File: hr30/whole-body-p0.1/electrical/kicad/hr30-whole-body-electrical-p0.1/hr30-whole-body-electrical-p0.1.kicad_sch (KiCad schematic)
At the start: 0 parts

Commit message: Expand HR-30 whole-body electrical architecture
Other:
- sheet 12 Head TTL, sensing, display and audio renamed 12 Head TTL, cameras, face display, audio and cooling
- added sheet 13 Auxiliary conversion and pelvis inertial sensing (13_pelvis_aux_imu.kicad_sch)
- added sheet 14 Left foot four-point load sensing (14_left_foot_load_sensing.kicad_sch)
- added sheet 15 Right foot four-point load sensing (15_right_foot_load_sensing.kicad_sch)

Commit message: Add pin-level HR-30 actuator interface carriers
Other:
- removed sheet 04 Five isolated RS-485 and three protected TTL interface channels
- removed sheet 05 Left-leg RS-485 and protected branch
- removed sheet 06 Right-leg RS-485 and protected branch
- removed sheet 07 Left proximal-arm RS-485 and protected branch
- removed sheet 08 Right proximal-arm RS-485 and protected branch
- removed sheet 09 Waist RS-485 and protected branch
- removed sheet 10 Left wrist/gripper TTL and protected branch
- removed sheet 11 Right wrist/gripper TTL and protected branch
- removed sheet 12 Head TTL, cameras, face display, audio and cooling
- removed sheet 13 Auxiliary conversion and pelvis inertial sensing
- removed sheet 14 Left foot four-point load sensing
- removed sheet 15 Right foot four-point load sensing
- added sheet 04 STM32H743 motion-controller power and carrier connectors (04_motion_controller_carrier_connectors.kicad_sch)
- added sheet 05 Carrier A - four isolated RS-485 channels (05_carrier_a_four_isolated_rs485.kicad_sch)
- added sheet 06 Carrier B - waist RS-485 and three translated TTL channels (06_carrier_b_waist_and_ttl.kicad_sch)
- added sheet 07 Left-leg RS-485 and protected branch (07_left_leg_rs485.kicad_sch)
- added sheet 08 Right-leg RS-485 and protected branch (08_right_leg_rs485.kicad_sch)
- added sheet 09 Left proximal-arm RS-485 and protected branch (09_left_arm_rs485.kicad_sch)
- added sheet 10 Right proximal-arm RS-485 and protected branch (10_right_arm_rs485.kicad_sch)
- added sheet 11 Waist RS-485 and protected branch (11_waist_rs485.kicad_sch)
- added sheet 12 Left wrist/gripper TTL and protected branch (12_left_distal_ttl.kicad_sch)
- added sheet 13 Right wrist/gripper TTL and protected branch (13_right_distal_ttl.kicad_sch)
- added sheet 14 Head TTL, cameras, face display, audio and cooling (14_head_ttl_sensors_hmi.kicad_sch)
- added sheet 15 Auxiliary conversion and pelvis inertial sensing (15_pelvis_aux_imu.kicad_sch)
- added sheet 16 Left foot four-point load sensing (16_left_foot_load_sensing.kicad_sch)
- added sheet 17 Right foot four-point load sensing (17_right_foot_load_sensing.kicad_sch)

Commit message: Correct HR-30 whole-body electrical architecture
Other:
- sheet 01 Energy, service disconnect, precharge and conversion renamed 01 Tether-first energy, regulated rails and onboard-later boundary
- sheet 07 Left-leg RS-485 and protected branch renamed 07 Left-leg RS-485 data bus and individual feeds
- sheet 08 Right-leg RS-485 and protected branch renamed 08 Right-leg RS-485 data bus and individual feeds
- sheet 09 Left proximal-arm RS-485 and protected branch renamed 09 Left proximal-arm RS-485 data bus and individual feeds
- sheet 10 Right proximal-arm RS-485 and protected branch renamed 10 Right proximal-arm RS-485 data bus and individual feeds
- sheet 11 Waist RS-485 and protected branch renamed 11 Waist RS-485 data bus and individual feed
- sheet 12 Left wrist/gripper TTL and protected branch renamed 12 Left wrist/gripper TTL data bus and individual feeds
- sheet 13 Right wrist/gripper TTL and protected branch renamed 13 Right wrist/gripper TTL data bus and individual feeds
- added sheet 18 Onboard-later isolated energy evaluation (18_onboard_later_energy_evaluation.kicad_sch)
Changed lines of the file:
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@@
           (exclude_from_sim no) (in_bom yes) (on_board yes) (dnp no)
           (stroke (width 0.5) (type solid)) (fill (color 0 0 0 0.0000))
-          (property "Sheetname" "01 Energy, service disconnect, precharge and conversion" (at 14.54 48.16 0) (effects (font (size 1.50 1.50)) (justify left bottom)))
+          (property "Sheetname" "01 Tether-first energy, regulated rails and onboard-later boundary" (at 14.54 48.16 0) (effects (font (size 1.50 1.50)) (justify left bottom)))
           (property "Sheetfile" "01_energy_precharge_conversion.kicad_sch" (at 14.54 63.40 0) (effects (font (size 1.30 1.30)) (justify left top)))
           (instances (project "hr30-whole-body-electrical-p0.1" (path "/6dbc6f1c-d05b-56f0-8b51-042e5f8599ba" (page "2"))))) (sheet (at 112.00 38.00) (size 92.0 40.64)
@@
           (exclude_from_sim no) (in_bom yes) (on_board yes) (dnp no)
           (stroke (width 0.5) (type solid)) (fill (color 0 0 0 0.0000))
-          (property "Sheetname" "07 Left-leg RS-485 and protected branch" (at 214.54 98.16 0) (effects (font (size 1.50 1.50)) (justify left bottom)))
+          (property "Sheetname" "07 Left-leg RS-485 data bus and individual feeds" (at 214.54 98.16 0) (effects (font (size 1.50 1.50)) (justify left bottom)))
           (property "Sheetfile" "07_left_leg_rs485.kicad_sch" (at 214.54 113.40 0) (effects (font (size 1.30 1.30)) (justify left top)))
           (instances (project "hr30-whole-body-electrical-p0.1" (path "/6dbc6f1c-d05b-56f0-8b51-042e5f8599ba" (page "8"))))) (sheet (at 312.00 88.00) (size 92.0 40.64)
           (exclude_from_sim no) (in_bom yes) (on_board yes) (dnp no)
           (stroke (width 0.5) (type solid)) (fill (color 0 0 0 0.0000))
-          (property "Sheetname" "08 Right-leg RS-485 and protected branch" (at 314.54 98.16 0) (effects (font (size 1.50 1.50)) (justify left bottom)))
+          (property "Sheetname" "08 Right-leg RS-485 data bus and individual feeds" (at 314.54 98.16 0) (effects (font (size 1.50 1.50)) (justify left bottom)))
           (property "Sheetfile" "08_right_leg_rs485.kicad_sch" (at 314.54 113.40 0) (effects (font (size 1.30 1.30)) (justify left top)))
           (instances (project "hr30-whole-body-electrical-p0.1" (path "/6dbc6f1c-d05b-56f0-8b51-042e5f8599ba" (page "9"))))) (sheet (at 12.00 138.00) (size 92.0 40.64)
           (exclude_from_sim no) (in_bom yes) (on_board yes) (dnp no)
           (stroke (width 0.5) (type solid)) (fill (color 0 0 0 0.0000))
-          (property "Sheetname" "09 Left proximal-arm RS-485 and protected branch" (at 14.54 148.16 0) (effects (font (size 1.50 1.50)) (justify left bottom)))
+          (property "Sheetname" "09 Left proximal-arm RS-485 data bus and individual feeds" (at 14.54 148.16 0) (effects (font (size 1.50 1.50)) (justify left bottom)))
           (property "Sheetfile" "09_left_arm_rs485.kicad_sch" (at 14.54 163.40 0) (effects (font (size 1.30 1.30)) (justify left top)))
           (instances (project "hr30-whole-body-electrical-p0.1" (path "/6dbc6f1c-d05b-56f0-8b51-042e5f8599ba" (page "10"))))) (sheet (at 112.00 138.00) (size 92.0 40.64)
           (exclude_from_sim no) (in_bom yes) (on_board yes) (dnp no)
           (stroke (width 0.5) (type solid)) (fill (color 0 0 0 0.0000))
-          (property "Sheetname" "10 Right proximal-arm RS-485 and protected branch" (at 114.54 148.16 0) (effects (font (size 1.50 1.50)) (justify left bottom)))
+          (property "Sheetname" "10 Right proximal-arm RS-485 data bus and individual feeds" (at 114.54 148.16 0) (effects (font (size 1.50 1.50)) (justify left bottom)))
           (property "Sheetfile" "10_right_arm_rs485.kicad_sch" (at 114.54 163.40 0) (effects (font (size 1.30 1.30)) (justify left top)))
           (instances (project "hr30-whole-body-electrical-p0.1" (path "/6dbc6f1c-d05b-56f0-8b51-042e5f8599ba" (page "11"))))) (sheet (at 212.00 138.00) (size 92.0 40.64)
           (exclude_from_sim no) (in_bom yes) (on_board yes) (dnp no)
           (stroke (width 0.5) (type solid)) (fill (color 0 0 0 0.0000))
-          (property "Sheetname" "11 Waist RS-485 and protected branch" (at 214.54 148.16 0) (effects (font (size 1.50 1.50)) (justify left bottom)))
+          (property "Sheetname" "11 Waist RS-485 data bus and individual feed" (at 214.54 148.16 0) (effects (font (size 1.50 1.50)) (justify left bottom)))
           (property "Sheetfile" "11_waist_rs485.kicad_sch" (at 214.54 163.40 0) (effects (font (size 1.30 1.30)) (justify left top)))
           (instances (project "hr30-whole-body-electrical-p0.1" (path "/6dbc6f1c-d05b-56f0-8b51-042e5f8599ba" (page "12"))))) (sheet (at 312.00 138.00) (size 92.0 40.64)
           (exclude_from_sim no) (in_bom yes) (on_board yes) (dnp no)
           (stroke (width 0.5) (type solid)) (fill (color 0 0 0 0.0000))
-          (property "Sheetname" "12 Left wrist/gripper TTL and protected branch" (at 314.54 148.16 0) (effects (font (size 1.50 1.50)) (justify left bottom)))
+          (property "Sheetname" "12 Left wrist/gripper TTL data bus and individual feeds" (at 314.54 148.16 0) (effects (font (size 1.50 1.50)) (justify left bottom)))
           (property "Sheetfile" "12_left_distal_ttl.kicad_sch" (at 314.54 163.40 0) (effects (font (size 1.30 1.30)) (justify left top)))
           (instances (project "hr30-whole-body-electrical-p0.1" (path "/6dbc6f1c-d05b-56f0-8b51-042e5f8599ba" (page "13"))))) (sheet (at 12.00 188.00) (size 92.0 40.64)
           (exclude_from_sim no) (in_bom yes) (on_board yes) (dnp no)
           (stroke (width 0.5) (type solid)) (fill (color 0 0 0 0.0000))
-          (property "Sheetname" "13 Right wrist/gripper TTL and protected branch" (at 14.54 198.16 0) (effects (font (size 1.50 1.50)) (justify left bottom)))
+          (property "Sheetname" "13 Right wrist/gripper TTL data bus and individual feeds" (at 14.54 198.16 0) (effects (font (size 1.50 1.50)) (justify left bottom)))
           (property "Sheetfile" "13_right_distal_ttl.kicad_sch" (at 14.54 213.40 0) (effects (font (size 1.30 1.30)) (justify left top)))
           (instances (project "hr30-whole-body-electrical-p0.1" (path "/6dbc6f1c-d05b-56f0-8b51-042e5f8599ba" (page "14"))))) (sheet (at 112.00 188.00) (size 92.0 40.64)
@@
           (property "Sheetname" "17 Right foot four-point load sensing" (at 14.54 248.16 0) (effects (font (size 1.50 1.50)) (justify left bottom)))
           (property "Sheetfile" "17_right_foot_load_sensing.kicad_sch" (at 14.54 263.40 0) (effects (font (size 1.30 1.30)) (justify left top)))
-          (instances (project "hr30-whole-body-electrical-p0.1" (path "/6dbc6f1c-d05b-56f0-8b51-042e5f8599ba" (page "18")))))
+          (instances (project "hr30-whole-body-electrical-p0.1" (path "/6dbc6f1c-d05b-56f0-8b51-042e5f8599ba" (page "18"))))) (sheet (at 112.00 238.00) (size 92.0 40.64)
+          (exclude_from_sim no) (in_bom yes) (on_board yes) (dnp no)
+          (stroke (width 0.5) (type solid)) (fill (color 0 0 0 0.0000))
+          (property "Sheetname" "18 Onboard-later isolated energy evaluation" (at 114.54 248.16 0) (effects (font (size 1.50 1.50)) (justify left bottom)))
+          (property "Sheetfile" "18_onboard_later_energy_evaluation.kicad_sch" (at 114.54 263.40 0) (effects (font (size 1.30 1.30)) (justify left top)))
+          (instances (project "hr30-whole-body-electrical-p0.1" (path "/6dbc6f1c-d05b-56f0-8b51-042e5f8599ba" (page "19")))))
   (sheet_instances (path "/" (page "1"))) (embedded_fonts no))

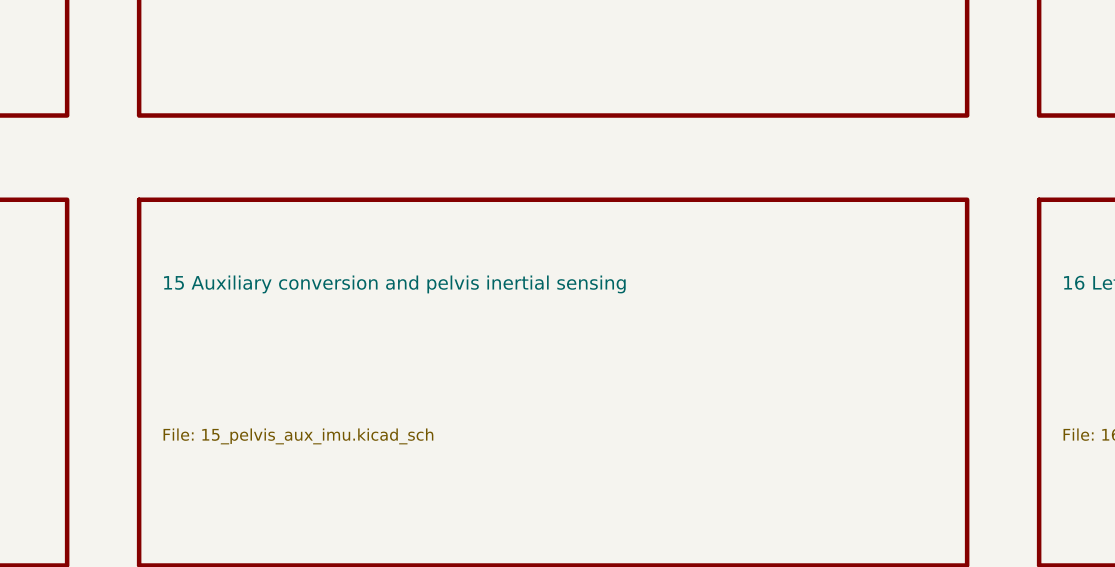
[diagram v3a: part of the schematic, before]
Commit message: Integrate HR-30 three-rail auxiliary power
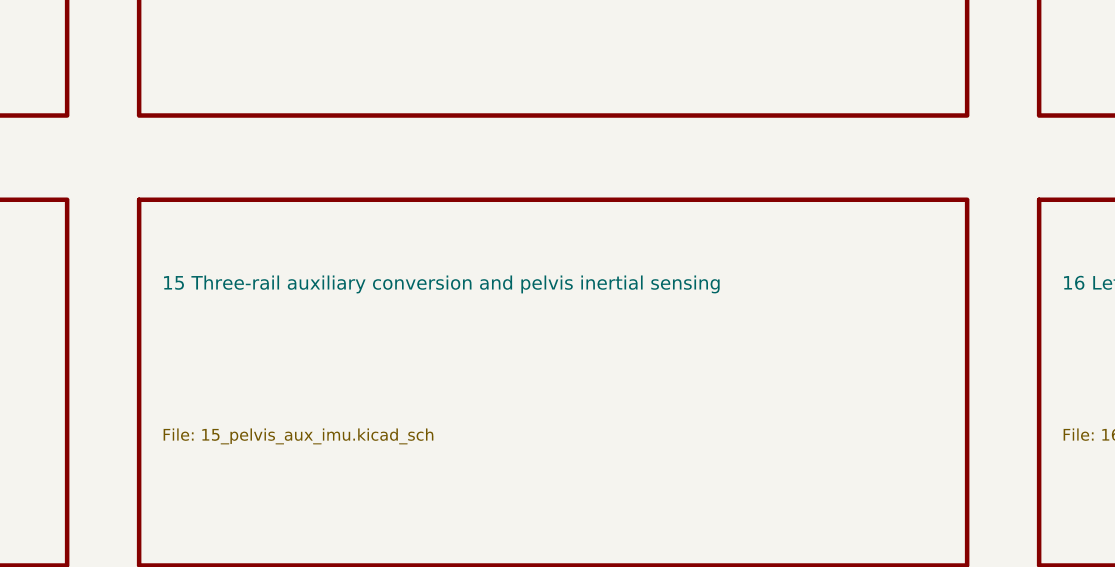
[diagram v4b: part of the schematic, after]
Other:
- sheet 15 Auxiliary conversion and pelvis inertial sensing renamed 15 Three-rail auxiliary conversion and pelvis inertial sensing
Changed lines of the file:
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@@
           (exclude_from_sim no) (in_bom yes) (on_board yes) (dnp no)
           (stroke (width 0.5) (type solid)) (fill (color 0 0 0 0.0000))
-          (property "Sheetname" "15 Auxiliary conversion and pelvis inertial sensing" (at 214.54 198.16 0) (effects (font (size 1.50 1.50)) (justify left bottom)))
+          (property "Sheetname" "15 Three-rail auxiliary conversion and pelvis inertial sensing" (at 214.54 198.16 0) (effects (font (size 1.50 1.50)) (justify left bottom)))
           (property "Sheetfile" "15_pelvis_aux_imu.kicad_sch" (at 214.54 213.40 0) (effects (font (size 1.30 1.30)) (justify left top)))
           (instances (project "hr30-whole-body-electrical-p0.1" (path "/6dbc6f1c-d05b-56f0-8b51-042e5f8599ba" (page "16"))))) (sheet (at 312.00 188.00) (size 92.0 40.64)
